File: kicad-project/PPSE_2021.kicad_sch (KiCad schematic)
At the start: 0 parts

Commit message: hw: add flash, switching circuit and XOUT resistor, change GPS and general cleanup
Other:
- title: (none) -> Main

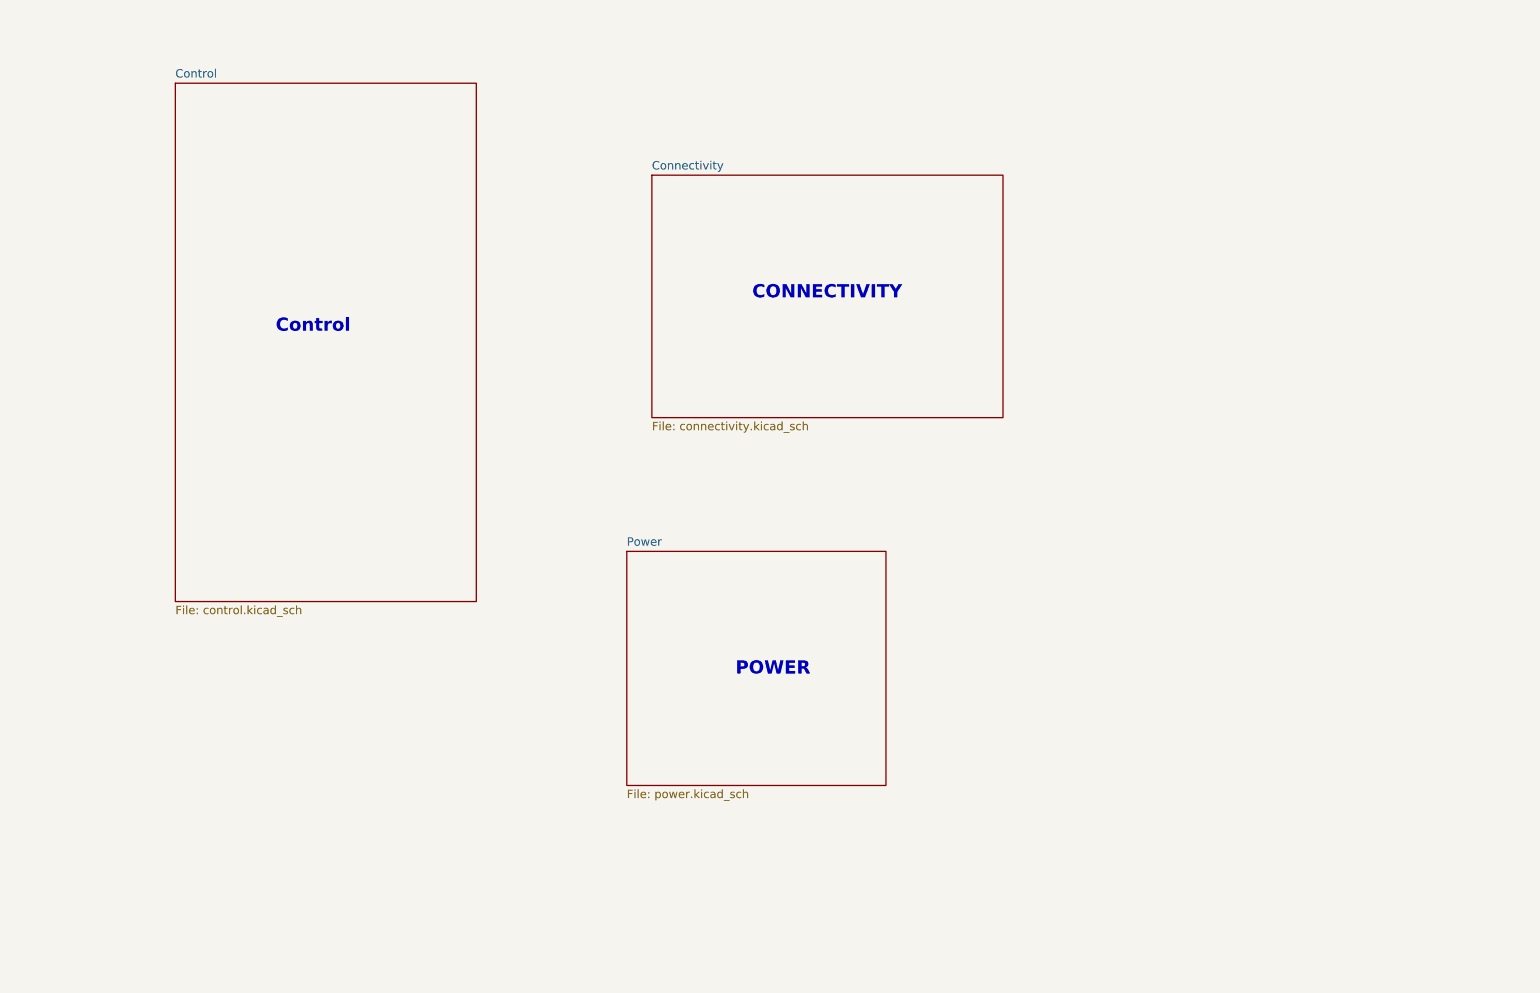
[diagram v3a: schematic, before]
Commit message: hw: add panel sensing and change GPS_EN to hierarchical pin
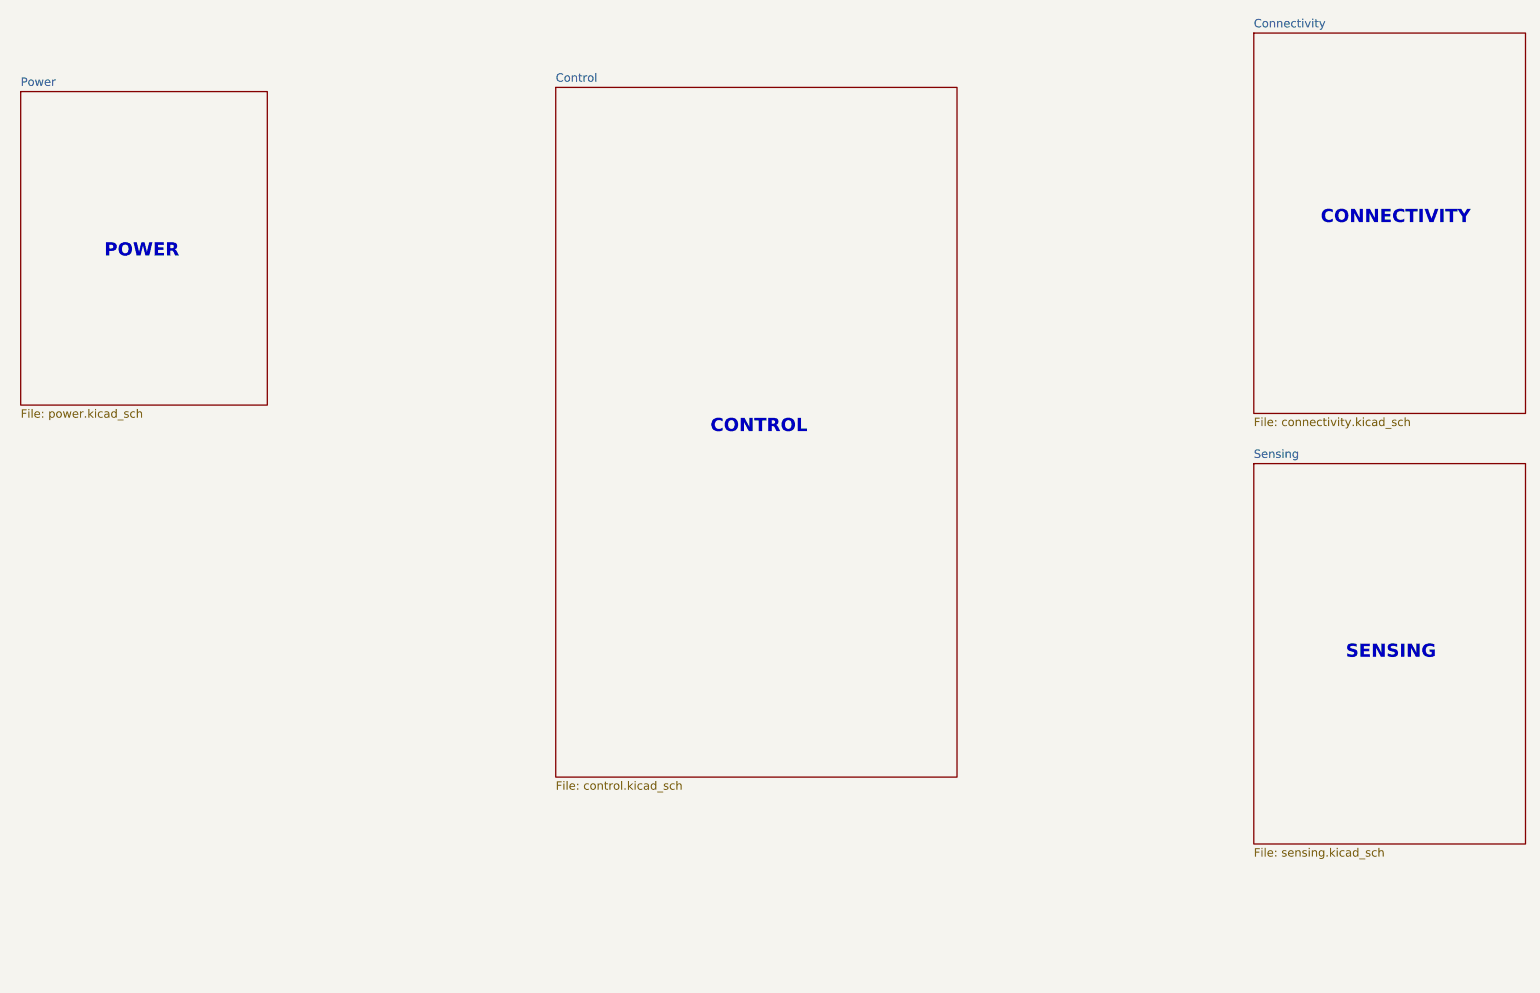
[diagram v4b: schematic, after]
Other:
- added sheet Sensing (sensing.kicad_sch)
- note added: "CONTROL"
- note added: "SENSING"
- note removed: "Control"
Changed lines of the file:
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@@
     (title "Main")
   )
-  (text "CONNECTIVITY" (at 138.43 72.39 0)
+  (text "CONNECTIVITY" (at 224.79 60.96 0)
     (effects (font (size 2.0066 2.0066) (thickness 0.4013) bold) (justify left bottom))
   )
-  (text "Control" (at 66.04 77.47 0)
+  (text "SENSING" (at 228.6 127 0)
     (effects (font (size 2.0066 2.0066) (thickness 0.4013) bold) (justify left bottom))
   )
-  (text "POWER" (at 135.89 129.54 0)
+  (text "CONTROL" (at 132.08 92.71 0)
     (effects (font (size 2.0066 2.0066) (thickness 0.4013) bold) (justify left bottom))
   )
-  (sheet (at 50.8 39.37) (size 45.72 78.74) (fields_autoplaced)
+  (text "POWER" (at 40.005 66.04 0)
+    (effects (font (size 2.0066 2.0066) (thickness 0.4013) bold) (justify left bottom))
+  )
+  (sheet (at 108.585 40.005) (size 60.96 104.775) (fields_autoplaced)
     (stroke (width 0) (type solid) (color 0 0 0 0))
     (fill (color 0 0 0 0.0000))
-    (property "Sheet name" "Control" (id 0) (at 50.8 38.6584 0)
+    (property "Sheet name" "Control" (id 0) (at 108.585 39.2934 0)
       (effects (font (size 1.27 1.27)) (justify left bottom))
     )
-    (property "Sheet file" "control.kicad_sch" (id 1) (at 50.8 118.6946 0)
+    (property "Sheet file" "control.kicad_sch" (id 1) (at 108.585 145.3646 0)
       (effects (font (size 1.27 1.27)) (justify left top))
     )
   )
-  (sheet (at 123.19 53.34) (size 53.34 36.83) (fields_autoplaced)
+  (sheet (at 214.63 31.75) (size 41.275 57.785) (fields_autoplaced)
     (stroke (width 0) (type solid) (color 0 0 0 0))
     (fill (color 0 0 0 0.0000))
-    (property "Sheet name" "Connectivity" (id 0) (at 123.19 52.6284 0)
+    (property "Sheet name" "Connectivity" (id 0) (at 214.63 31.0384 0)
       (effects (font (size 1.27 1.27)) (justify left bottom))
     )
-    (property "Sheet file" "connectivity.kicad_sch" (id 1) (at 123.19 90.7546 0)
+    (property "Sheet file" "connectivity.kicad_sch" (id 1) (at 214.63 90.1196 0)
       (effects (font (size 1.27 1.27)) (justify left top))
     )
   )
-  (sheet (at 119.38 110.49) (size 39.37 35.56) (fields_autoplaced)
+  (sheet (at 27.305 40.64) (size 37.465 47.625) (fields_autoplaced)
     (stroke (width 0) (type solid) (color 0 0 0 0))
     (fill (color 0 0 0 0.0000))
-    (property "Sheet name" "Power" (id 0) (at 119.38 109.7784 0)
+    (property "Sheet name" "Power" (id 0) (at 27.305 39.9284 0)
       (effects (font (size 1.27 1.27)) (justify left bottom))
     )
-    (property "Sheet file" "power.kicad_sch" (id 1) (at 119.38 146.6346 0)
+    (property "Sheet file" "power.kicad_sch" (id 1) (at 27.305 88.8496 0)
+      (effects (font (size 1.27 1.27)) (justify left top))
+    )
+  )
+  (sheet (at 214.63 97.155) (size 41.275 57.785) (fields_autoplaced)
+    (stroke (width 0.1524) (type solid) (color 0 0 0 0))
+    (fill (color 0 0 0 0.0000))
+    (property "Sheet name" "Sensing" (id 0) (at 214.63 96.4434 0)
+      (effects (font (size 1.27 1.27)) (justify left bottom))
+    )
+    (property "Sheet file" "sensing.kicad_sch" (id 1) (at 214.63 155.5246 0)
       (effects (font (size 1.27 1.27)) (justify left top))
     )
@@
     (path "/00000000-0000-0000-0000-0000622d0e2d" (page "3"))
     (path "/00000000-0000-0000-0000-0000622b4158" (page "4"))
+    (path "/e92ed148-d831-4ee6-93c4-e593d47b2e2f" (page "5"))
   )
   (symbol_instances
@@
       (reference "#PWR?") (unit 1) (value "+3V3") (footprint "")
     )
+    (path "/e92ed148-d831-4ee6-93c4-e593d47b2e2f/0f8c049a-74aa-49fb-88e0-8100b529cb45"
+      (reference "#PWR?") (unit 1) (value "GND") (footprint "")
+    )
+    (path "/e92ed148-d831-4ee6-93c4-e593d47b2e2f/178096a9-355f-4b77-b895-9470d785b3ba"
+      (reference "#PWR?") (unit 1) (value "GND") (footprint "")
+    )
     (path "/00000000-0000-0000-0000-00006222e27b/18392ba2-c872-4bc7-8742-8d9474d292c4"
       (reference "#PWR?") (unit 1) (value "GND") (footprint "")
@@
     )
     (path "/00000000-0000-0000-0000-0000622d0e2d/283644c8-e504-4d29-ac28-692c64f7a922"
+      (reference "#PWR?") (unit 1) (value "+3V3") (footprint "")
+    )
+    (path "/e92ed148-d831-4ee6-93c4-e593d47b2e2f/2add4251-7da1-4e81-92e5-4d6bad9b3c37"
       (reference "#PWR?") (unit 1) (value "+3V3") (footprint "")
     )
@@
       (reference "#PWR?") (unit 1) (value "+3V3") (footprint "")
     )
+    (path "/e92ed148-d831-4ee6-93c4-e593d47b2e2f/b18046a2-5005-4f1e-a713-909235ac1cf4"
+      (reference "#PWR?") (unit 1) (value "GND") (footprint "")
+    )
     (path "/00000000-0000-0000-0000-00006222e27b/b1b8f7ab-a25c-4411-a2ae-6a61f24e870f"
       (reference "#PWR?") (unit 1) (value "GND") (footprint "")
@@
     (path "/00000000-0000-0000-0000-00006222e27b/d410b46c-f7fd-4361-b9e2-92339d04ec0f"
       (reference "#PWR?") (unit 1) (value "GND") (footprint "")
+    )
+    (path "/e92ed148-d831-4ee6-93c4-e593d47b2e2f/d5e7cf8a-fcd8-49f5-bb5b-891a7b7e4c5f"
+      (reference "#PWR?") (unit 1) (value "+3V3") (footprint "")
     )
     (path "/00000000-0000-0000-0000-0000622d0e2d/da14c723-3458-4fa6-bc5d-30313bed2338"
@@
       (reference "#PWR?") (unit 1) (value "+12V") (footprint "")
     )
+    (path "/e92ed148-d831-4ee6-93c4-e593d47b2e2f/e0b4cafa-07e3-4fa9-85d2-3fad5b17429e"
+      (reference "#PWR?") (unit 1) (value "GND") (footprint "")
+    )
     (path "/00000000-0000-0000-0000-00006222e27b/e4a1a699-249b-4fa7-9d26-ace0601b3c82"
       (reference "#PWR?") (unit 1) (value "GND") (footprint "")
@@
       (reference "J?") (unit 1) (value "Screw_Terminal_01x02") (footprint "")
     )
+    (path "/e92ed148-d831-4ee6-93c4-e593d47b2e2f/d971ee45-43a3-4243-ac16-a8c40ad35aa9"
+      (reference "J?") (unit 1) (value "Screw_Terminal_01x04") (footprint "")
+    )
     (path "/00000000-0000-0000-0000-00006222e27b/7d84260a-fa22-4d79-8c7a-214c2c72161d"
       (reference "JP?") (unit 1) (value "SolderJumper_2_Open") (footprint "")
@@
       (reference "R?") (unit 1) (value "1k") (footprint "")
     )
+    (path "/e92ed148-d831-4ee6-93c4-e593d47b2e2f/4eecb6f5-b080-4f5f-9bcf-d4e05c93c37f"
+      (reference "R?") (unit 1) (value "R") (footprint "")
+    )
+    (path "/e92ed148-d831-4ee6-93c4-e593d47b2e2f/54d69e97-f940-46ae-8662-3a15059a9bdf"
+      (reference "R?") (unit 1) (value "R") (footprint "")
+    )
+    (path "/e92ed148-d831-4ee6-93c4-e593d47b2e2f/77974df4-9826-4ef7-b829-5d6faf385f24"
+      (reference "R?") (unit 1) (value "R") (footprint "")
+    )
     (path "/00000000-0000-0000-0000-00006222e27b/80198411-a019-4296-9154-9c0df7fa049d"
       (reference "R?") (unit 1) (value "1k") (footprint "")
     )
+    (path "/e92ed148-d831-4ee6-93c4-e593d47b2e2f/a739816b-c26a-41f0-b6a4-af8e06388273"
+      (reference "R?") (unit 1) (value "R") (footprint "")
+    )
+    (path "/e92ed148-d831-4ee6-93c4-e593d47b2e2f/c7a7b759-bfd8-4247-969b-3a8d42e65385"
+      (reference "R?") (unit 1) (value "R") (footprint "")
+    )
+    (path "/e92ed148-d831-4ee6-93c4-e593d47b2e2f/cfb676d4-7ad2-4e96-b314-65db38ece868"
+      (reference "R?") (unit 1) (value "R_Shunt") (footprint "")
+    )
     (path "/00000000-0000-0000-0000-0000622d0e2d/e691ce7c-7910-49cf-b230-0ea8e1b30f6e"
       (reference "R?") (unit 1) (value "1k") (footprint "")
     )
+    (path "/e92ed148-d831-4ee6-93c4-e593d47b2e2f/eb288f72-e17f-441a-a95d-d989994ed43d"
+      (reference "R?") (unit 1) (value "R") (footprint "")
+    )
     (path "/00000000-0000-0000-0000-00006222e27b/f6b96e8d-3422-4b74-8627-5d7f566a7ffe"
       (reference "R?") (unit 1) (value "DNP 10k") (footprint "")
@@
       (reference "U?") (unit 1) (value "PAM-7Q-0") (footprint "PAM7Q0")
     )
+    (path "/e92ed148-d831-4ee6-93c4-e593d47b2e2f/bc523eca-d9b5-40c2-8f8f-203aeb42c34d"
+      (reference "U?") (unit 1) (value "OPAMP") (footprint "")
+    )
     (path "/00000000-0000-0000-0000-00006222e27b/c9428947-9de7-4ab0-b30d-b8cff1508223"
       (reference "U?") (unit 1) (value "W25Q16JVSS") (footprint "Package_SO:SOIC-8_5.23x5.23mm_P1.27mm")
     )
+    (path "/e92ed148-d831-4ee6-93c4-e593d47b2e2f/d90cb12e-ea8c-4cf1-9dce-f67d7a85eea7"
+      (reference "U?") (unit 1) (value "OPAMP") (footprint "")
+    )
     (path "/00000000-0000-0000-0000-00006222e27b/b0aa0484-92ab-41af-b89f-b78a70ba8ef0"

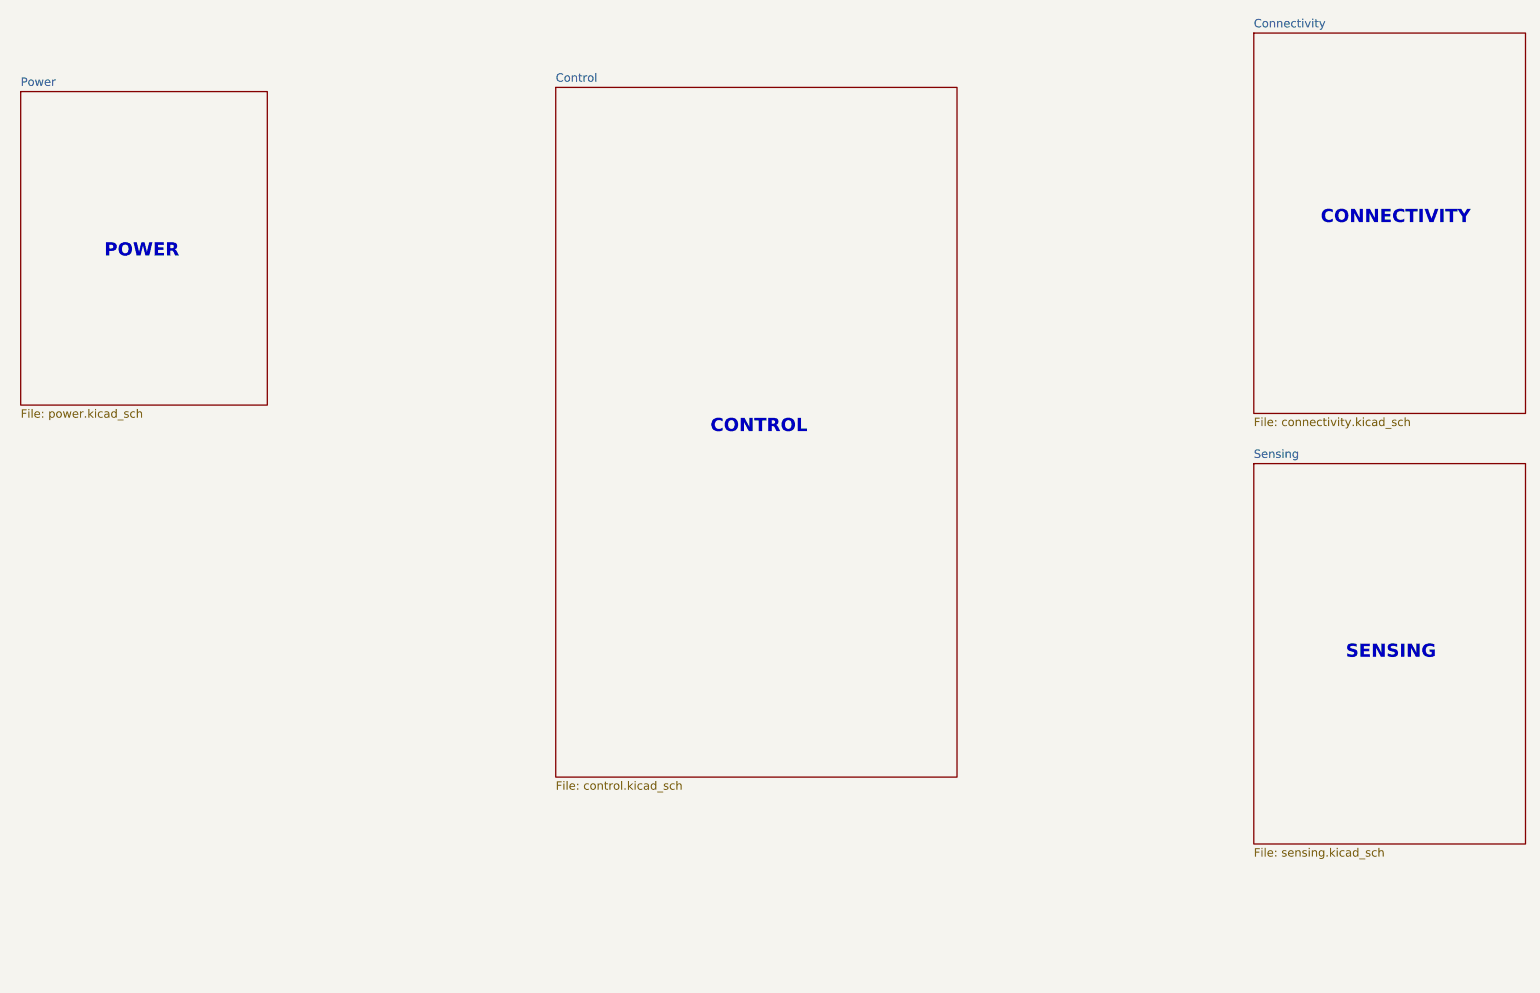
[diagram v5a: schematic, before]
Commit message: hw: add limit switches, dual power input, actuation sheet, debug and expansion connectors and connect sheets
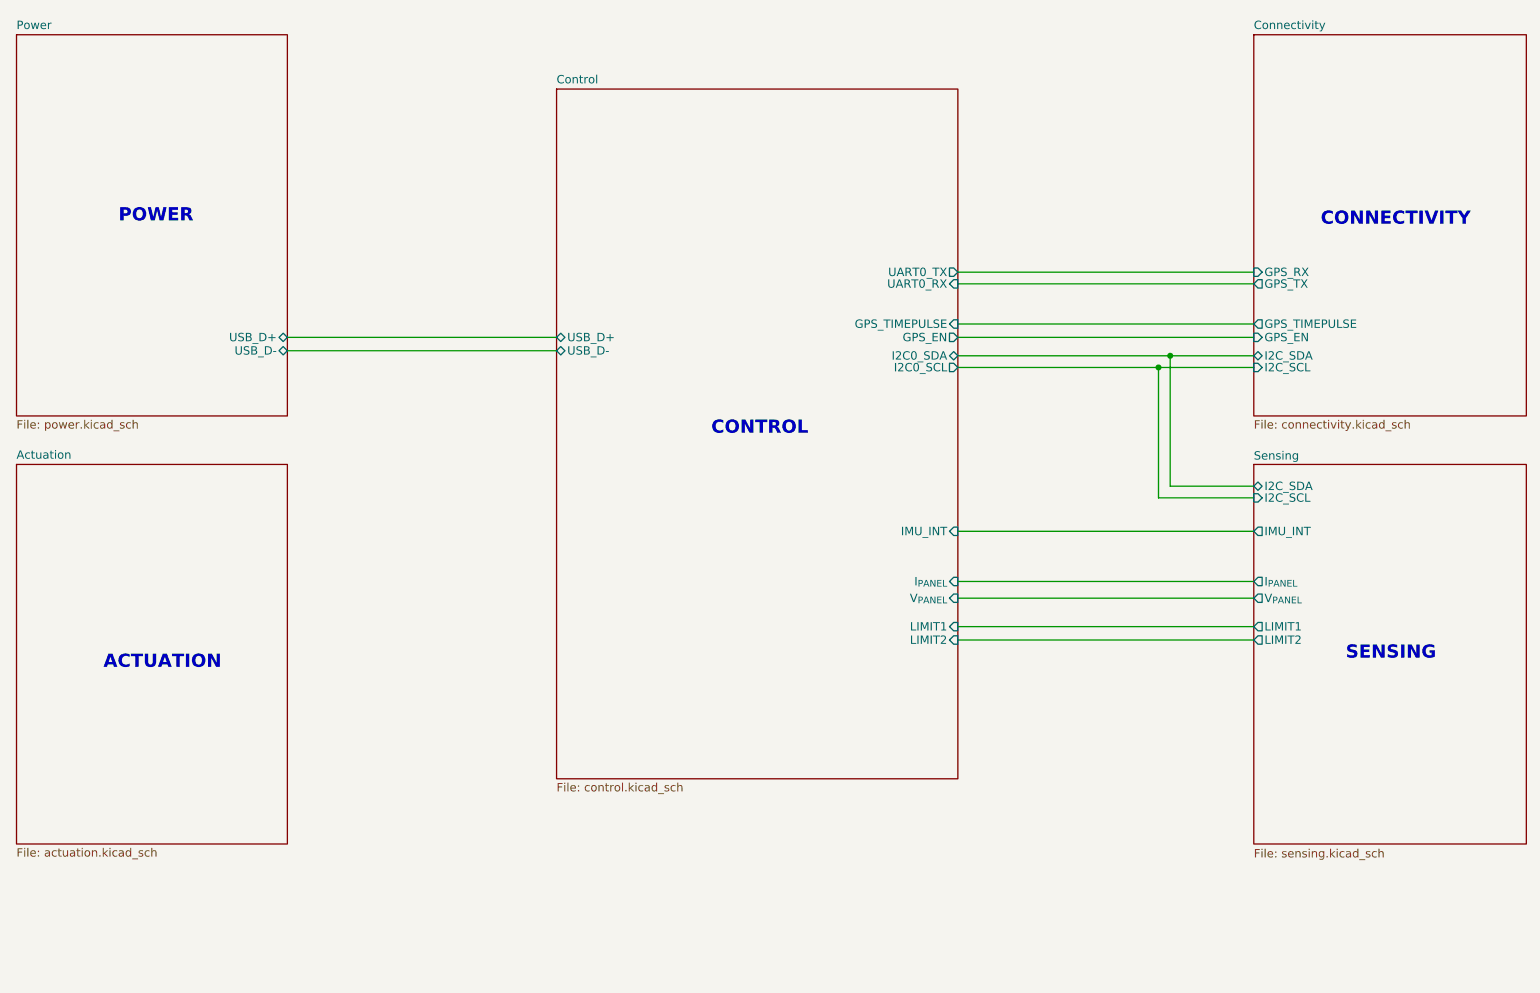
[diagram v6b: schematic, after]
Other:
- added sheet Actuation (actuation.kicad_sch)
- sheet Connectivity ports: added GPS_EN, GPS_RX, GPS_TIMEPULSE, GPS_TX, I2C_SCL, I2C_SDA; removed none
- sheet Control ports: added GPS_EN, GPS_TIMEPULSE, I2C0_SCL, I2C0_SDA, IMU_INT, I_{PANEL}, LIMIT1, LIMIT2, UART0_RX, UART0_TX, USB_D+, USB_D-, V_{PANEL}; removed none
- sheet Power ports: added USB_D+, USB_D-; removed none
- sheet Sensing ports: added I2C_SCL, I2C_SDA, IMU_INT, I_{PANEL}, LIMIT1, LIMIT2, V_{PANEL}; removed none
- note added: "ACTUATION"

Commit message: hw: schematic updates
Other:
- sheet Sensing ports: added none; removed I2C_SCL, I2C_SDA
- note added: "Allineamento griglia grullo, rifare."
- note added: "Dato alim. switching vogliamo prevedere anche delle ferrite bead nelle alim. degli integrati?"
